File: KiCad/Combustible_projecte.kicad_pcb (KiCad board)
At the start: 2 copper layers, 125.5 x 75.5 mm, 60 parts, among them J1 DE9_Pins, J2 DE9_Pins, J20 Conn_01x02, J3 Conn_01x05, J4 Conn_01x02, J5 Conn_01x02, J6 Conn_01x02, Q1 2N7002, Q2 2N7002, SW1 SW_Push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

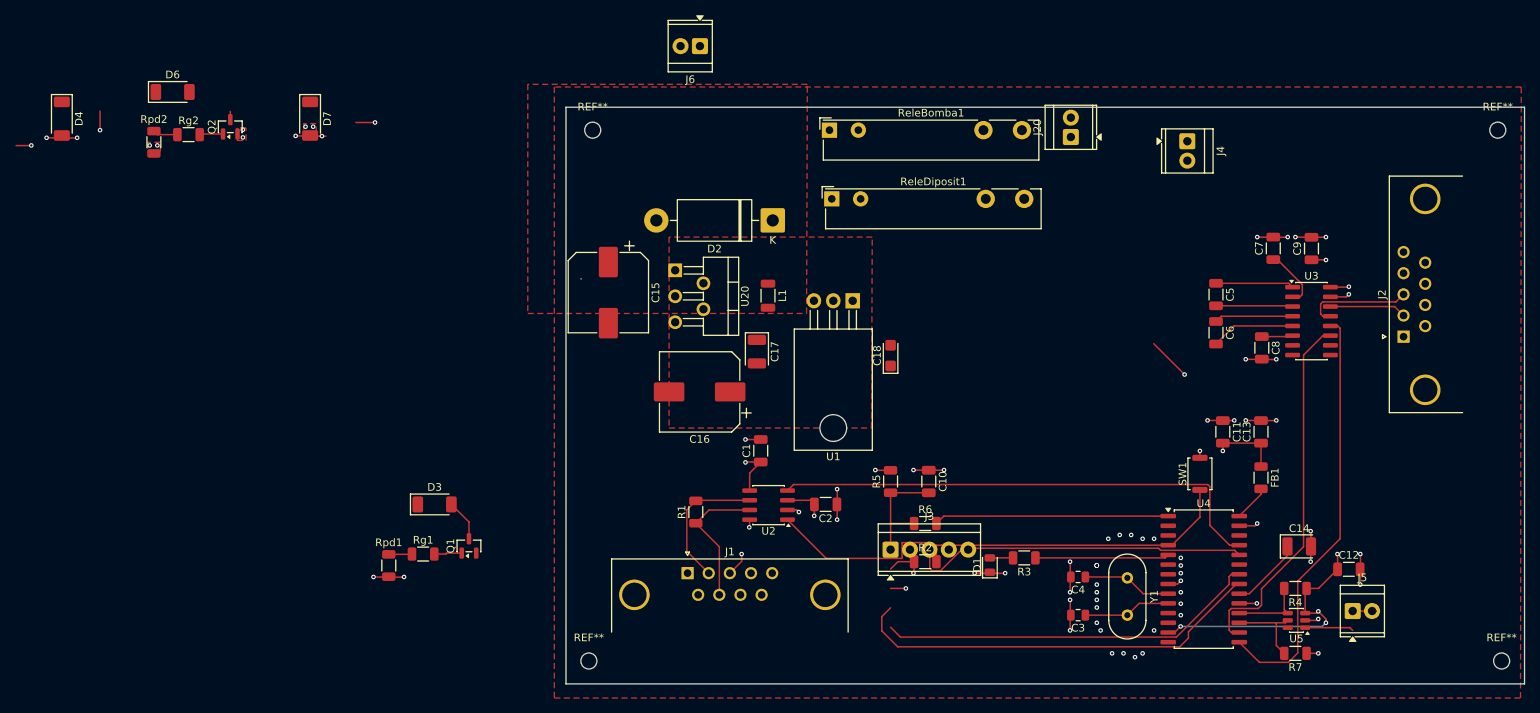
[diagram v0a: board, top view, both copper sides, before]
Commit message: pcb bastant canviada i actualitzada
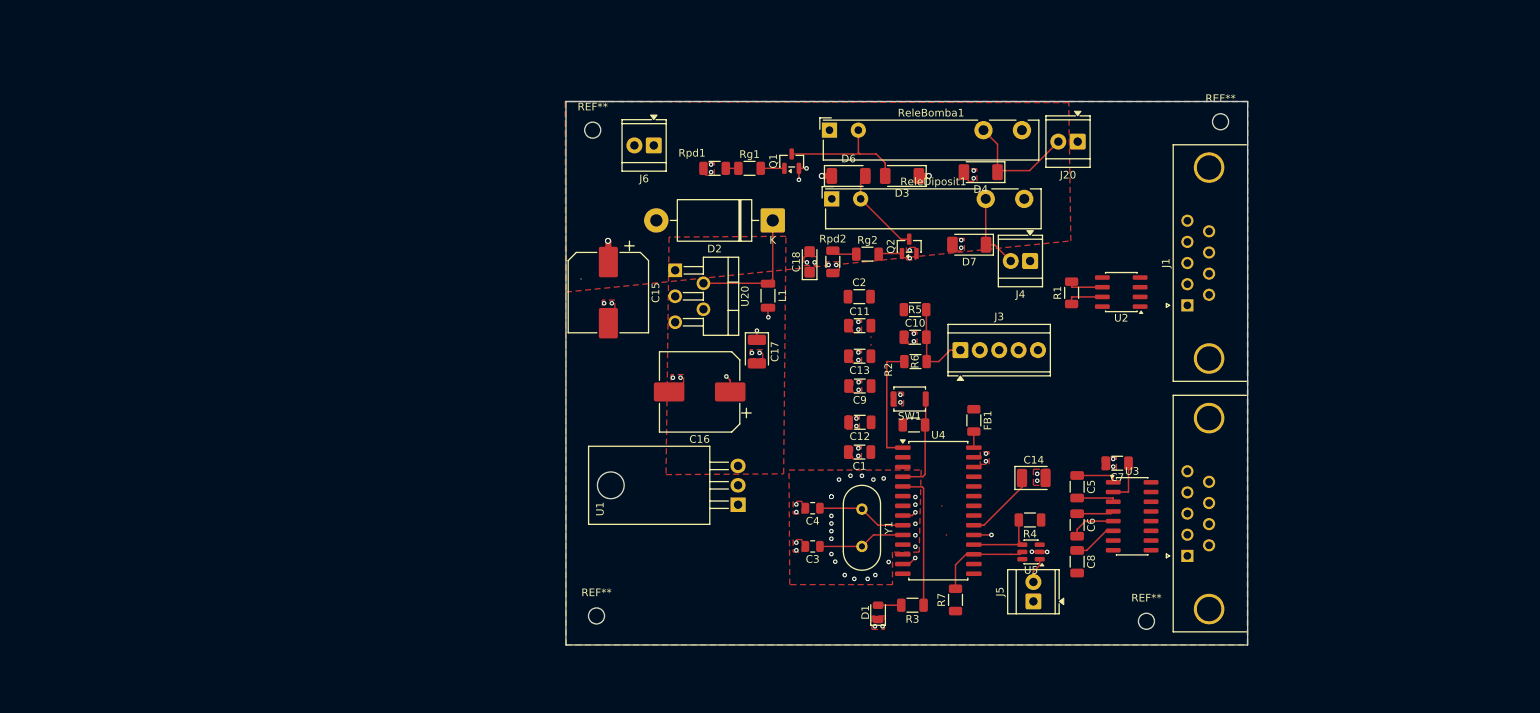
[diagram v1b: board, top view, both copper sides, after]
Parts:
- moved D4 120.5 mm to (109.3, 31.5), turned to 180 degrees
- moved Q2 90.3 mm to (99.9, 41.2)
- moved Rpd2 90.3 mm to (89.9, 43.2)
- moved Rg2 90.3 mm to (94.5, 42.2)
- moved D6 89.2 mm to (92.0, 32.0)
- moved D7 87.9 mm to (107.8, 41.0), turned to 180 degrees
- moved D3 74.8 mm to (99.0, 32.0), turned to 180 degrees
- moved J1 74.2 mm to (136.4, 48.9), turned to 90 degrees
- moved Rpd1 67.3 mm to (74.5, 31.0), turned to 180 degrees
- moved C12 66.9 mm to (93.5, 64.2), turned to 180 degrees
- moved Rg1 66.2 mm to (79.0, 31.0)
- moved Q1 65.7 mm to (84.5, 30.1)
- moved C9 61.8 mm to (93.5, 59.5), turned to 180 degrees
- moved R1 57.0 mm to (121.2, 47.3)
- moved U2 53.9 mm to (127.7, 47.2)
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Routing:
- net GND: track 91.1 -> 8.83 mm, vias 76 -> 74
- net 3v3: track 75.2 -> 3.27 mm, vias 13 -> 1
- net CAN_TX: track 68.3 -> 0.00 mm
- net CAN_RX: track 65.7 -> 0.00 mm
- net USART_RX: track 55.5 -> 0.00 mm
- net PGD: track 55.0 -> 0.03 mm
- net PGC: track 50.2 -> 0.04 mm
- net USART_TX: track 48.2 -> 0.00 mm
- net RBO: track 41.8 -> 13.0 mm
- net Net-(D2-K): track 0.00 -> 17.0 mm
- net Bomba_combustible: track 0.00 -> 15.9 mm
- net Net-(U4-/MCLR): track 30.8 -> 15.7 mm
- net R1_IN: track 14.1 -> 0.00 mm
- net CAN_L: track 18.2 -> 4.75 mm
- net CAN_H: track 18.4 -> 4.95 mm
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- added copper zone on B.Cu, net GND
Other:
- board size 125.5 x 75.5 mm -> 89.2 x 71.2 mm

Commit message: Rotuing acabat? falta les regles del fabricant
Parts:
- moved U2 2.56 mm to (129.4, 49.1)
- moved R1 2.56 mm to (122.9, 49.2)
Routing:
- net USART_TX: track 0.00 -> 38.2 mm
- net CAN_RX: track 0.00 -> 35.8 mm
- net USART_RX: track 0.00 -> 34.8 mm
- net CAN_TX: track 0.00 -> 32.9 mm
- net PGD: track 0.03 -> 28.0 mm
- net PGC: track 0.04 -> 27.9 mm
- net CAN_H: track 4.95 -> 29.8 mm
- net CAN_L: track 4.75 -> 19.7 mm
- net T1_OUT: track 0.00 -> 10.9 mm
- net R1_IN: track 0.00 -> 4.88 mm
- net 3v3: track 3.27 -> 6.17 mm, vias 1 -> 2
- net GND: track 8.83 -> 7.00 mm, vias 74 -> 79
- net VBAT: track 5.39 -> 4.09 mm, vias 3 -> 2
